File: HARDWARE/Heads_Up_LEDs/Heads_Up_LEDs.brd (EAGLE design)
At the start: 160 x 35.2 mm, 4 parts, among them J1 AUDIO_JACK_TRRSSMD_RA

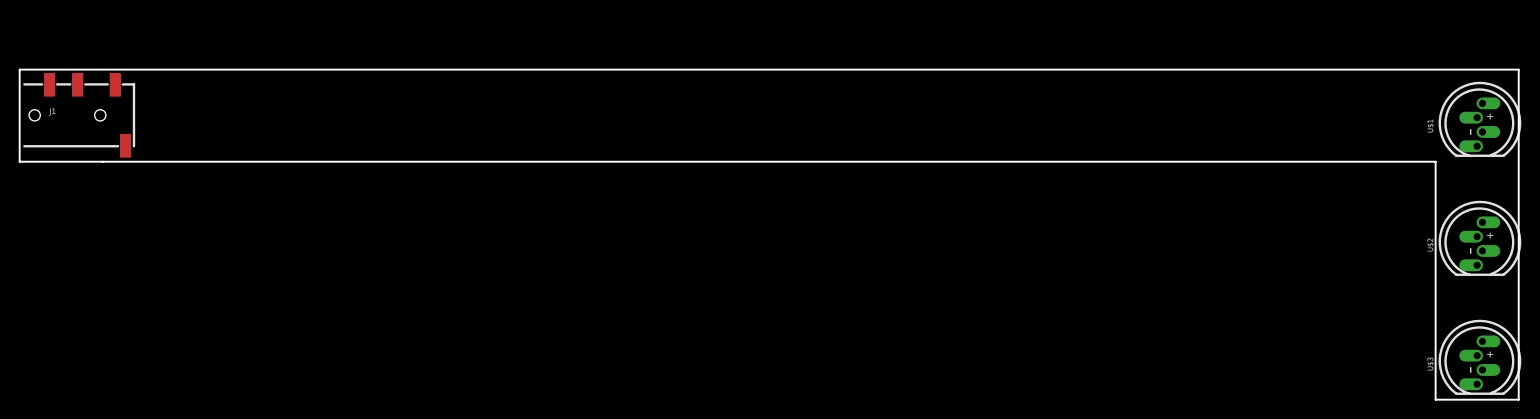
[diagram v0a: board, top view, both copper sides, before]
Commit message: heads up leds with ws2812s - v01
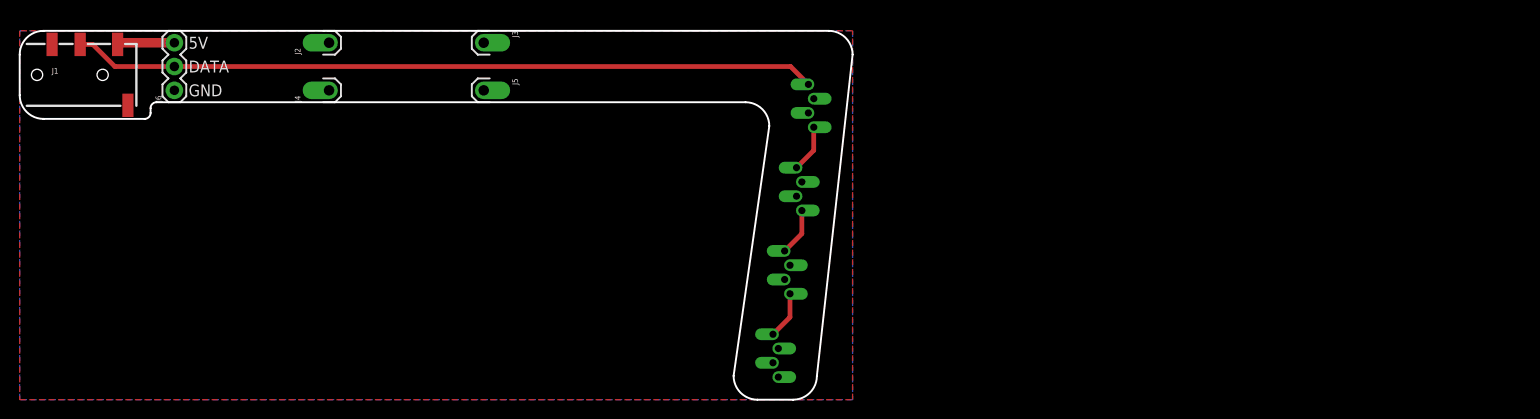
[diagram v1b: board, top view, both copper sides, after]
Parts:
- added J2, J3, J4, J5: (no value), SparkFun-Connectors:1X01_OFFSET
- added J6: (no value), SparkFun-Connectors:1X03
- added U$4: WS2812B-PTH, SparkFun-LED:WS2812B-PTH-KIT
- J1: value AUDIO_JACK_TRRSSMD_RA -> TRRS
- moved U$3 76.6 mm to (84.8, 31.5), flipped to the bottom, turned to 270 degrees
- moved U$1 75.5 mm to (82.3, 13.7), flipped to the bottom, turned to 270 degrees
- moved U$2 72.9 mm to (83.6, 22.6), flipped to the bottom, turned to 270 degrees
- moved J1 4.33 mm to (0.25, 34.7)
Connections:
- new net 5V: J1.TIP, J6.3, U$1.3, U$2.3, U$3.3, U$4.3
- new net DATA: J1.RING1, J6.2, U$3.4
- new net GND: J1.EARTH, J1.RING2, J6.1, U$1.2, U$2.2, U$3.2, U$4.2
- new net N$1: U$1.1, U$4.4
- new net N$7: U$2.4, U$3.1
- new net N$8: U$1.4, U$2.1
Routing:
- net DATA: track 0.00 -> 79.5 mm
- net 5V: track 0.00 -> 6.24 mm
- net N$7: track 0.00 -> 5.08 mm
- net N$8: track 0.00 -> 5.08 mm
- net N$1: track 0.00 -> 5.07 mm
- added copper zone on layer 16, net 5V
- added copper zone on layer 1, net GND
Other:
- board size 160 x 35.2 mm -> 88.9 x 39.4 mm
- board text added: "5V"
- board text added: "DATA"
- board text added: "GND"
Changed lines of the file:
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@@
 <setting verticaltext="up"/>
 </settings>
-<grid distance="50" unitdist="mil" unit="inch" style="dots" multiple="1" display="yes" altdistance="5" altunitdist="mil" altunit="inch"/>
+<grid distance="50" unitdist="mil" unit="inch" style="dots" multiple="1" display="yes" altdistance="0.001" altunitdist="inch" altunit="inch"/>
 <layers>
 <layer number="1" name="Top" color="4" fill="1" visible="yes" active="yes"/>
@@
 <board>
 <plain>
-<wire x1="0" y1="25.4" x2="8.89" y2="25.4" width="0.2032" layer="20"/>
-<wire x1="8.89" y1="25.4" x2="151.13" y2="25.4" width="0.2032" layer="20"/>
-<wire x1="151.13" y1="25.4" x2="151.13" y2="0" width="0.2032" layer="20"/>
-<wire x1="151.13" y1="0" x2="160" y2="0" width="0.2032" layer="20"/>
-<wire x1="160" y1="0" x2="160" y2="35.23" width="0.2032" layer="20"/>
-<wire x1="160" y1="35.23" x2="0" y2="35.23" width="0.2032" layer="20"/>
-<wire x1="0" y1="35.23" x2="0" y2="25.4" width="0.2032" layer="20"/>
+<wire x1="0" y1="36.83" x2="0" y2="32.512" width="0.2032" layer="20"/>
+<wire x1="0" y1="32.512" x2="2.54" y2="29.972" width="0.2032" layer="20" curve="90"/>
+<wire x1="2.54" y1="29.972" x2="13.335" y2="29.972" width="0.2032" layer="20"/>
+<wire x1="13.335" y1="29.972" x2="13.97" y2="30.607" width="0.2032" layer="20" curve="90"/>
+<wire x1="13.97" y1="30.607" x2="13.97" y2="31.115" width="0.2032" layer="20"/>
+<wire x1="13.97" y1="31.115" x2="14.605" y2="31.75" width="0.2032" layer="20" curve="-90"/>
+<wire x1="14.605" y1="31.75" x2="77.47" y2="31.75" width="0.2032" layer="20"/>
+<wire x1="77.47" y1="31.75" x2="80.01" y2="29.21" width="0.2032" layer="20" curve="-90"/>
+<wire x1="80.01" y1="29.21" x2="76.2" y2="2.54" width="0.2032" layer="20"/>
+<wire x1="76.2" y1="2.54" x2="78.74" y2="0" width="0.2032" layer="20" curve="90"/>
+<wire x1="78.74" y1="0" x2="82.55" y2="0" width="0.2032" layer="20"/>
+<wire x1="82.55" y1="0" x2="85.09" y2="2.54" width="0.2032" layer="20" curve="90"/>
+<wire x1="85.09" y1="2.54" x2="88.9" y2="36.83" width="0.2032" layer="20"/>
+<wire x1="88.9" y1="36.83" x2="86.36" y2="39.37" width="0.2032" layer="20" curve="90"/>
+<wire x1="86.36" y1="39.37" x2="2.54" y2="39.37" width="0.2032" layer="20"/>
+<wire x1="2.54" y1="39.37" x2="0" y2="36.83" width="0.2032" layer="20" curve="90"/>
+<text x="18.034" y="37.465" size="1.27" layer="21" font="vector" ratio="13">5V</text>
+<text x="18.034" y="32.385" size="1.27" layer="21" font="vector" ratio="13">GND</text>
+<text x="18.034" y="34.925" size="1.27" layer="21" font="vector" ratio="13">DATA</text>
 </plain>
 <attributes>
@@
 </autorouter>
 <elements>
-<element name="J1" library="SparkFun-Connectors" package="AUDIO_JACK_3.5MM_TRRS_SMD_RA" value="AUDIO_JACK_TRRSSMD_RA" x="0" y="30.353">
-<attribute name="PROD_ID" value="CONN-10676" x="0" y="30.353" size="1.778" layer="27" display="off"/>
-<attribute name="SF_ID" value="PRT-12639" x="0" y="30.353" size="1.778" layer="27" display="off"/>
+<element name="J1" library="SparkFun-Connectors" package="AUDIO_JACK_3.5MM_TRRS_SMD_RA" value="TRRS" x="0.254" y="34.671">
+<attribute name="PROD_ID" value="CONN-10676" x="0.254" y="34.671" size="1.778" layer="27" display="off"/>
+<attribute name="SF_ID" value="PRT-12639" x="0.254" y="34.671" size="1.778" layer="27" display="off"/>
 </element>
-<element name="U$1" library="SparkFun-LED" package="WS2812B-PTH-KIT" value="WS2812B-PTH" x="156.21" y="29.21" rot="R90"/>
-<element name="U$2" library="SparkFun-LED" package="WS2812B-PTH-KIT" value="WS2812B-PTH" x="156.21" y="16.51" rot="R90"/>
-<element name="U$3" library="SparkFun-LED" package="WS2812B-PTH-KIT" value="WS2812B-PTH" x="156.21" y="3.81" rot="R90"/>
+<element name="U$1" library="SparkFun-LED" package="WS2812B-PTH-KIT" value="WS2812B-PTH" x="82.296" y="13.716" rot="MR270"/>
+<element name="U$2" library="SparkFun-LED" package="WS2812B-PTH-KIT" value="WS2812B-PTH" x="83.566" y="22.606" rot="MR270"/>
+<element name="U$3" library="SparkFun-LED" package="WS2812B-PTH-KIT" value="WS2812B-PTH" x="84.836" y="31.496" rot="MR270"/>
+<element name="J2" library="SparkFun-Connectors" package="1X01_OFFSET" value="" x="33.02" y="38.1" rot="R90"/>
+<element name="J3" library="SparkFun-Connectors" package="1X01_OFFSET" value="" x="49.53" y="38.1" rot="R270"/>
+<element name="J4" library="SparkFun-Connectors" package="1X01_OFFSET" value="" x="33.02" y="33.02" rot="R90"/>
+<element name="J5" library="SparkFun-Connectors" package="1X01_OFFSET" value="" x="49.53" y="33.02" rot="R270"/>
+<element name="J6" library="SparkFun-Connectors" package="1X03" value="" x="16.51" y="33.02" rot="R90">
+<attribute name="PROD_ID" value="XXX-00000" x="16.51" y="33.02" size="1.778" layer="27" rot="R90" display="off"/>
+</element>
+<element name="U$4" library="SparkFun-LED" package="WS2812B-PTH-KIT" value="WS2812B-PTH" x="81.0514" y="4.826" rot="MR270"/>
 </elements>
 <signals>
+<signal name="N$7">
+<contactref element="U$3" pad="1"/>
+<contactref element="U$2" pad="4"/>
+<wire x1="84.7566" y1="29.083" x2="84.7566" y2="26.6065" width="0.508" layer="1"/>
+<wire x1="84.7566" y1="26.6065" x2="82.9151" y2="24.765" width="0.508" layer="1"/>
+</signal>
+<signal name="N$8">
+<contactref element="U$2" pad="1"/>
+<contactref element="U$1" pad="4"/>
+<wire x1="83.4866" y1="20.193" x2="83.4866" y2="17.7165" width="0.508" layer="1"/>
+<wire x1="83.4866" y1="17.7165" x2="81.6451" y2="15.875" width="0.508" layer="1"/>
+</signal>
+<signal name="5V">
+<contactref element="U$3" pad="3"/>
+<contactref element="U$2" pad="3"/>
+<contactref element="U$1" pad="3"/>
+<contactref element="J6" pad="3"/>
+<polygon width="0.1524" layer="16" isolate="0.3048">
+<vertex x="0" y="0"/>
+<vertex x="0" y="39.37"/>
+<vertex x="88.9" y="39.37"/>
+<vertex x="88.9" y="0"/>
+</polygon>
+<contactref element="J1" pad="TIP"/>
+<wire x1="10.454" y1="37.921" x2="10.454" y2="38.1" width="1.016" layer="1"/>
+<wire x1="10.454" y1="38.1" x2="16.51" y2="38.1" width="1.016" layer="1"/>
+<contactref element="U$4" pad="3"/>
+</signal>
+<signal name="GND">
+<contactref element="U$3" pad="2"/>
+<contactref element="U$2" pad="2"/>
+<contactref element="U$1" pad="2"/>
+<polygon width="0.1524" layer="1" isolate="0.3048">
+<vertex x="0" y="0"/>
+<vertex x="88.9" y="0"/>
+<vertex x="88.9" y="39.37"/>
+<vertex x="0" y="39.37"/>
+</polygon>
+<contactref element="J1" pad="EARTH"/>
+<contactref element="J1" pad="RING2"/>
+<contactref element="J6" pad="1"/>
+<contactref element="U$4" pad="2"/>
+</signal>
+<signal name="DATA">
+<contactref element="U$3" pad="4"/>
+<contactref element="J6" pad="2"/>
+<contactref element="J1" pad="RING1"/>
+<wire x1="6.454" y1="37.921" x2="7.799" y2="37.921" width="0.508" layer="1"/>
+<wire x1="7.799" y1="37.921" x2="10.16" y2="35.56" width="0.508" layer="1"/>
+<wire x1="10.16" y1="35.56" x2="16.51" y2="35.56" width="0.508" layer="1"/>
+<wire x1="16.51" y1="35.56" x2="82.2801" y2="35.56" width="0.508" layer="1"/>
+<wire x1="82.2801" y1="35.56" x2="84.1851" y2="33.655" width="0.508" layer="1"/>
+</signal>
+<signal name="N$1">
+<contactref element="U$1" pad="1"/>
+<contactref element="U$4" pad="4"/>
+<wire x1="82.2166" y1="8.8011" x2="80.4005" y2="6.985" width="0.508" layer="1"/>
+<wire x1="82.2166" y1="11.303" x2="82.2166" y2="8.8011" width="0.508" layer="1"/>
+</signal>
 </signals>
 <mfgpreviewcolors>

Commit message: fixed ws2812 pinouts - added res and cap
library for ws2812 pth pinout was incorrect. I also added in a cap and resistor like the hookup guide suggests. Not sure if necessary, cuz the protos of v01 are working without (although I had to rotate the LEDs 180 degrees.
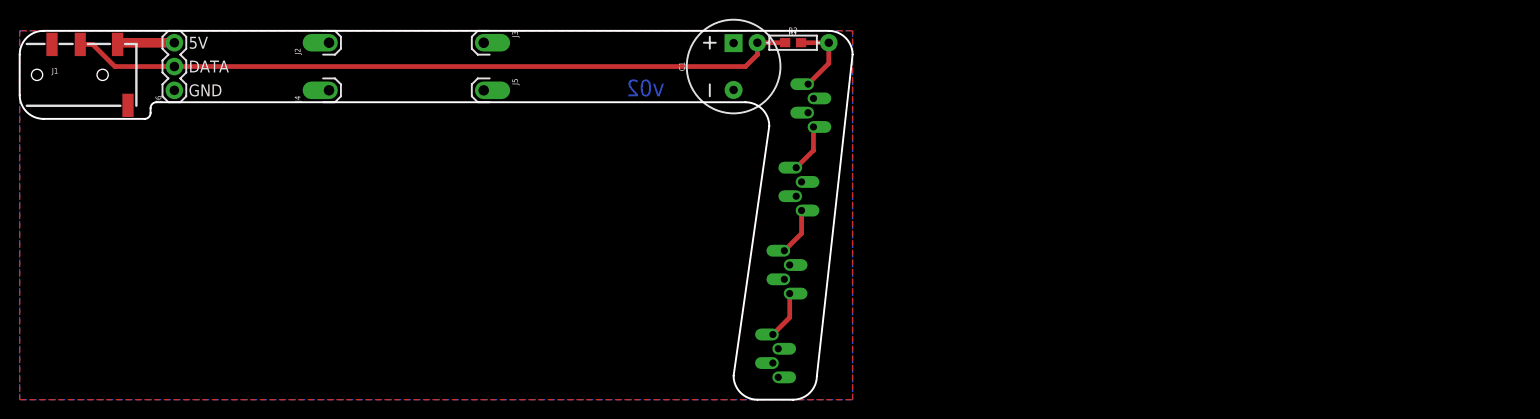
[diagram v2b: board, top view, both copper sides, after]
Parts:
- added C1: 1mF, SparkFun-Capacitors:CPOL-RADIAL-5MM-10MM
- added R1: 300, SparkFun-Resistors:0603
- added R2: (no value), SparkFun-Resistors:AXIAL-0.3
- moved U$2 0.80 mm to (82.8, 22.4), turned to 90 degrees
- moved U$1 0.80 mm to (81.5, 13.5), turned to 90 degrees
- moved U$3 0.80 mm to (84.1, 31.3), turned to 90 degrees
- moved U$4 0.79 mm to (80.3, 4.55), turned to 90 degrees
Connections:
- new net N$2: R1.2, R2.P$2, U$3.1
- net 5V: now also C1.+, U$1.2, U$2.2, U$3.2, U$4.2; no longer U$1.3, U$2.3, U$3.3, U$4.3
- net DATA: now also R1.1, R2.P$1; no longer U$3.4
- net GND: now also C1.-, U$1.3, U$2.3, U$3.3, U$4.3; no longer U$1.2, U$2.2, U$3.2, U$4.2
- net N$1: now also U$1.4, U$4.1; no longer U$1.1, U$4.4
- net N$7: now also U$2.1, U$3.4; no longer U$2.4, U$3.1
- net N$8: now also U$1.1, U$2.4; no longer U$1.4, U$2.1
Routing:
- net N$2: track 0.00 -> 8.29 mm
- net DATA: track 79.5 -> 78.0 mm
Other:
- board text added: "v02"
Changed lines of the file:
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@@
 <text x="18.034" y="32.385" size="1.27" layer="21" font="vector" ratio="13">GND</text>
 <text x="18.034" y="34.925" size="1.27" layer="21" font="vector" ratio="13">DATA</text>
+<text x="68.834" y="32.385" size="1.778" layer="16" font="vector" ratio="13" rot="MR0">v02</text>
 </plain>
 <attributes>
@@
 <attribute name="SF_ID" value="PRT-12639" x="0.254" y="34.671" size="1.778" layer="27" display="off"/>
 </element>
-<element name="U$1" library="SparkFun-LED" package="WS2812B-PTH-KIT" value="WS2812B-PTH" x="82.296" y="13.716" rot="MR270"/>
-<element name="U$2" library="SparkFun-LED" package="WS2812B-PTH-KIT" value="WS2812B-PTH" x="83.566" y="22.606" rot="MR270"/>
-<element name="U$3" library="SparkFun-LED" package="WS2812B-PTH-KIT" value="WS2812B-PTH" x="84.836" y="31.496" rot="MR270"/>
+<element name="U$1" library="SparkFun-LED" package="WS2812B-PTH-KIT" value="WS2812B-PTH" x="81.534" y="13.4874" rot="MR90"/>
+<element name="U$2" library="SparkFun-LED" package="WS2812B-PTH-KIT" value="WS2812B-PTH" x="82.804" y="22.352" rot="MR90"/>
+<element name="U$3" library="SparkFun-LED" package="WS2812B-PTH-KIT" value="WS2812B-PTH" x="84.074" y="31.2674" rot="MR90"/>
 <element name="J2" library="SparkFun-Connectors" package="1X01_OFFSET" value="" x="33.02" y="38.1" rot="R90"/>
 <element name="J3" library="SparkFun-Connectors" package="1X01_OFFSET" value="" x="49.53" y="38.1" rot="R270"/>
@@
 <attribute name="PROD_ID" value="XXX-00000" x="16.51" y="33.02" size="1.778" layer="27" rot="R90" display="off"/>
 </element>
-<element name="U$4" library="SparkFun-LED" package="WS2812B-PTH-KIT" value="WS2812B-PTH" x="81.0514" y="4.826" rot="MR270"/>
+<element name="U$4" library="SparkFun-LED" package="WS2812B-PTH-KIT" value="WS2812B-PTH" x="80.3148" y="4.5466" rot="MR90"/>
+<element name="R1" library="SparkFun-Resistors" package="0603" value="300" x="82.55" y="38.1">
+<attribute name="PROD_ID" value="RES_10328" x="82.55" y="38.1" size="1.778" layer="27" font="vector" ratio="13" display="off"/>
+</element>
+<element name="R2" library="SparkFun-Resistors" package="AXIAL-0.3" value=" " x="82.55" y="38.1">
+<attribute name="PROD_ID" value=" " x="82.55" y="38.1" size="1.778" layer="27" font="vector" ratio="13" display="off"/>
+</element>
+<element name="C1" library="SparkFun-Capacitors" package="CPOL-RADIAL-5MM-10MM" value="1mF" x="76.2" y="35.56" rot="R90">
+<attribute name="PROD_ID" value="CAP-09538" x="76.2" y="35.56" size="1.778" layer="27" font="vector" ratio="13" rot="R90" display="off"/>
+</element>
 </elements>
 <signals>
 <signal name="N$7">
-<contactref element="U$3" pad="1"/>
+<contactref element="U$3" pad="4"/>
+<contactref element="U$2" pad="1"/>
+<wire x1="84.7249" y1="29.1084" x2="84.7249" y2="26.6065" width="0.508" layer="1"/>
+<wire x1="84.7249" y1="26.6065" x2="82.8834" y2="24.765" width="0.508" layer="1"/>
+</signal>
+<signal name="N$8">
 <contactref element="U$2" pad="4"/>
-<wire x1="84.7566" y1="29.083" x2="84.7566" y2="26.6065" width="0.508" layer="1"/>
-<wire x1="84.7566" y1="26.6065" x2="82.9151" y2="24.765" width="0.508" layer="1"/>
-</signal>
-<signal name="N$8">
-<contactref element="U$2" pad="1"/>
-<contactref element="U$1" pad="4"/>
-<wire x1="83.4866" y1="20.193" x2="83.4866" y2="17.7165" width="0.508" layer="1"/>
-<wire x1="83.4866" y1="17.7165" x2="81.6451" y2="15.875" width="0.508" layer="1"/>
+<contactref element="U$1" pad="1"/>
+<wire x1="83.4549" y1="20.193" x2="83.4549" y2="17.7419" width="0.508" layer="1"/>
+<wire x1="83.4549" y1="17.7419" x2="81.6134" y2="15.9004" width="0.508" layer="1"/>
 </signal>
 <signal name="5V">
-<contactref element="U$3" pad="3"/>
-<contactref element="U$2" pad="3"/>
-<contactref element="U$1" pad="3"/>
+<contactref element="U$3" pad="2"/>
+<contactref element="U$2" pad="2"/>
+<contactref element="U$1" pad="2"/>
 <contactref element="J6" pad="3"/>
 <polygon width="0.1524" layer="16" isolate="0.3048">
@@
 <wire x1="10.454" y1="37.921" x2="10.454" y2="38.1" width="1.016" layer="1"/>
 <wire x1="10.454" y1="38.1" x2="16.51" y2="38.1" width="1.016" layer="1"/>
-<contactref element="U$4" pad="3"/>
+<contactref element="U$4" pad="2"/>
+<contactref element="C1" pad="+"/>
 </signal>
 <signal name="GND">
-<contactref element="U$3" pad="2"/>
-<contactref element="U$2" pad="2"/>
-<contactref element="U$1" pad="2"/>
+<contactref element="U$3" pad="3"/>
+<contactref element="U$2" pad="3"/>
+<contactref element="U$1" pad="3"/>
 <polygon width="0.1524" layer="1" isolate="0.3048">
 <vertex x="0" y="0"/>
@@
 <contactref element="J1" pad="RING2"/>
 <contactref element="J6" pad="1"/>
-<contactref element="U$4" pad="2"/>
+<contactref element="U$4" pad="3"/>
+<contactref element="C1" pad="-"/>
 </signal>
 <signal name="DATA">
-<contactref element="U$3" pad="4"/>
 <contactref element="J6" pad="2"/>
 <contactref element="J1" pad="RING1"/>
@@
 <wire x1="7.799" y1="37.921" x2="10.16" y2="35.56" width="0.508" layer="1"/>
 <wire x1="10.16" y1="35.56" x2="16.51" y2="35.56" width="0.508" layer="1"/>
-<wire x1="16.51" y1="35.56" x2="82.2801" y2="35.56" width="0.508" layer="1"/>
-<wire x1="82.2801" y1="35.56" x2="84.1851" y2="33.655" width="0.508" layer="1"/>
+<contactref element="R1" pad="1"/>
+<contactref element="R2" pad="P$1"/>
+<wire x1="81.7" y1="38.1" x2="78.74" y2="38.1" width="0.508" layer="1"/>
+<wire x1="77.47" y1="35.56" x2="78.74" y2="36.83" width="0.508" layer="1"/>
+<wire x1="78.74" y1="36.83" x2="78.74" y2="38.1" width="0.508" layer="1"/>
+<wire x1="16.51" y1="35.56" x2="77.47" y2="35.56" width="0.508" layer="1"/>
 </signal>
 <signal name="N$1">
-<contactref element="U$1" pad="1"/>
-<contactref element="U$4" pad="4"/>
-<wire x1="82.2166" y1="8.8011" x2="80.4005" y2="6.985" width="0.508" layer="1"/>
-<wire x1="82.2166" y1="11.303" x2="82.2166" y2="8.8011" width="0.508" layer="1"/>
+<contactref element="U$1" pad="4"/>
+<contactref element="U$4" pad="1"/>
+<wire x1="82.1849" y1="11.3284" x2="82.1849" y2="8.7503" width="0.508" layer="1"/>
+<wire x1="82.1849" y1="8.7503" x2="80.3942" y2="6.9596" width="0.508" layer="1"/>
+</signal>
+<signal name="N$2">
+<contactref element="U$3" pad="1"/>
+<contactref element="R1" pad="2"/>
+<contactref element="R2" pad="P$2"/>
+<wire x1="84.1534" y1="33.6804" x2="86.36" y2="35.887" width="0.508" layer="1"/>
+<wire x1="86.36" y1="35.887" x2="86.36" y2="38.1" width="0.508" layer="1"/>
+<wire x1="86.36" y1="38.1" x2="83.4" y2="38.1" width="0.508" layer="1"/>
 </signal>
 </signals>
